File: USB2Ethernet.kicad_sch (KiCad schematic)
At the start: 35 parts, among them U17 LAN9512, U19 CAT250xxx, Y6 25Mhz

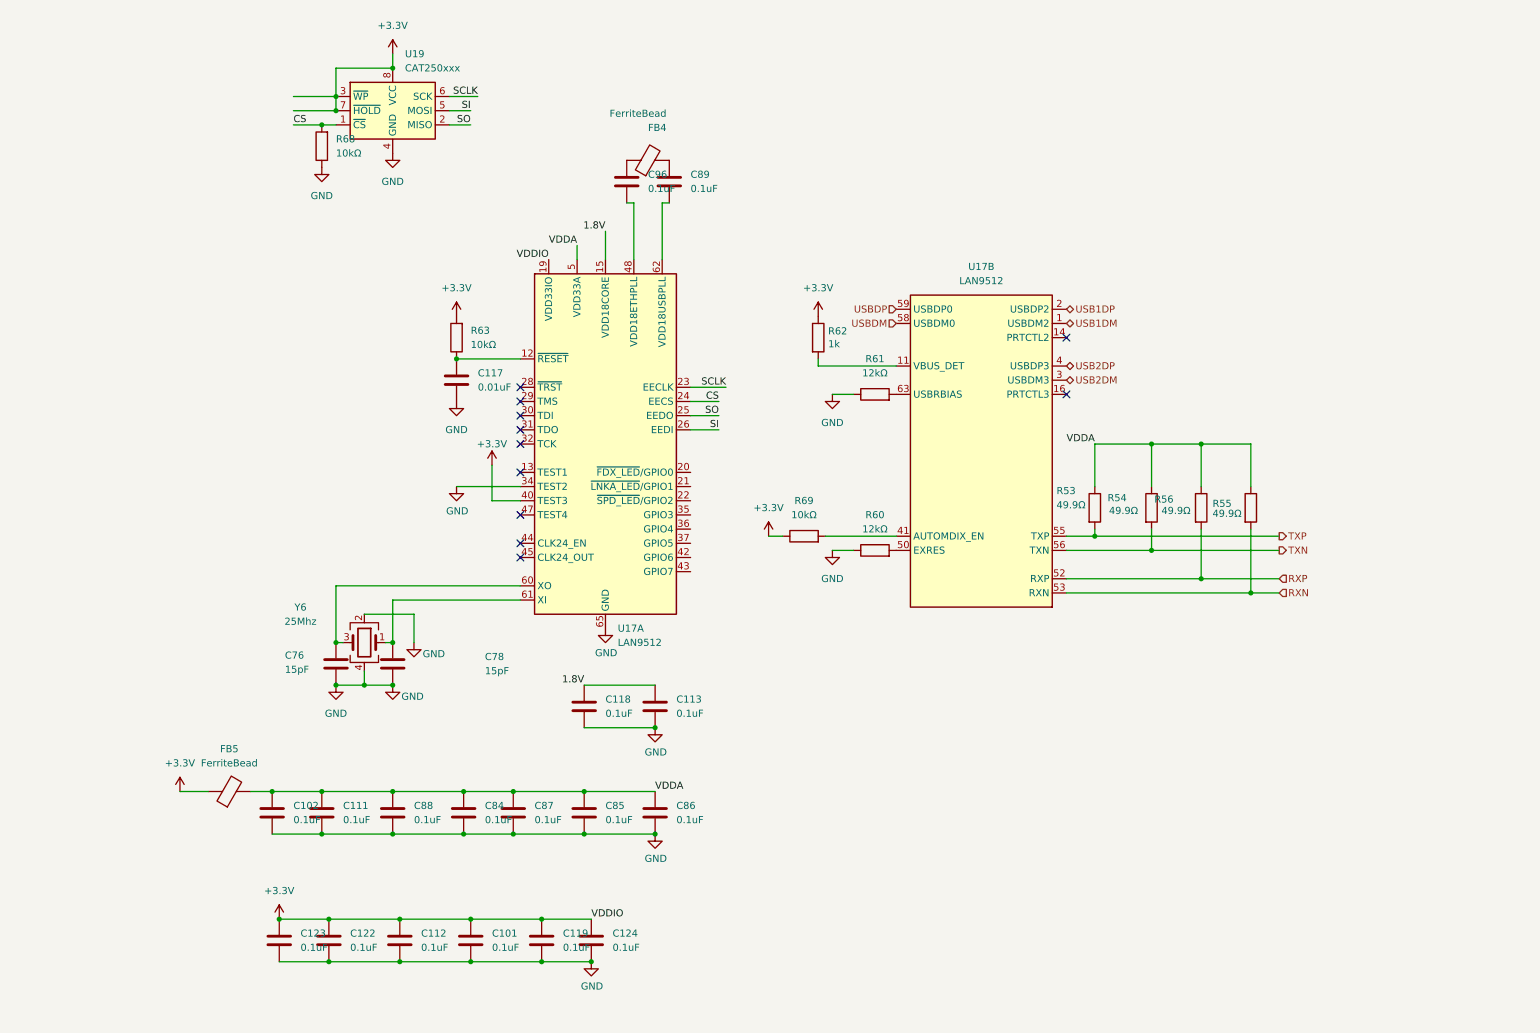
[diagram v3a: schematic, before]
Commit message: add sata capacitor
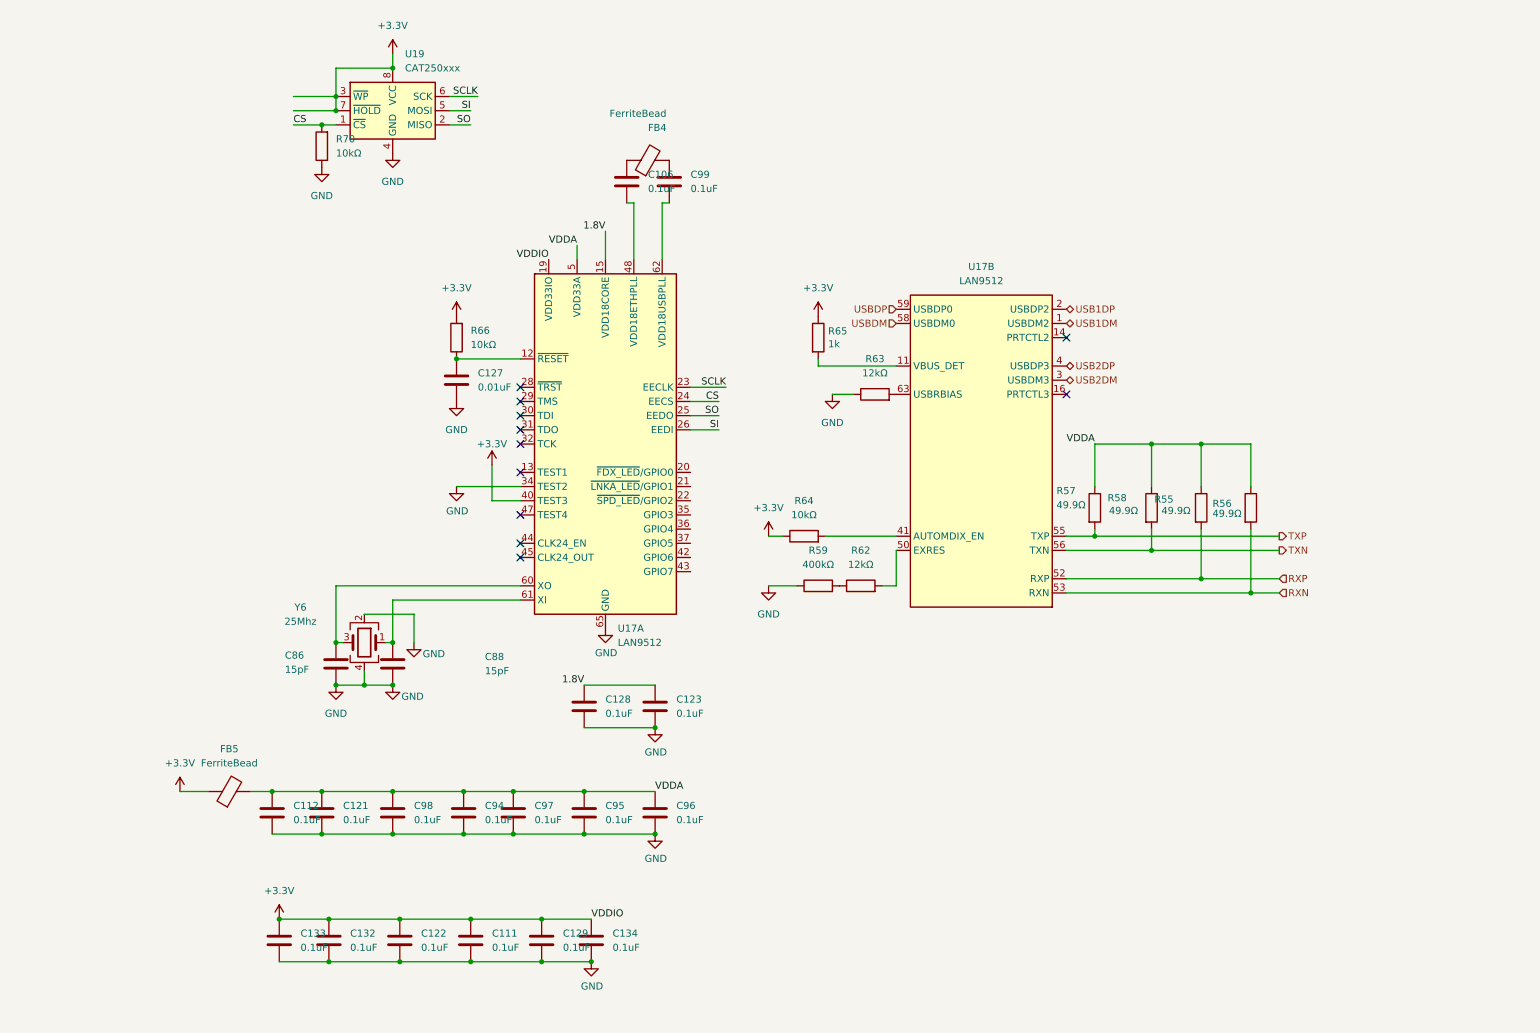
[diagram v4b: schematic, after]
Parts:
- added R59: 400kΩ, Resistor_SMD:R_0603_1608Metric_Pad0.98x0.95mm_HandSolder, symbol Device:R
- renumbered C96 to C106, C101 to C111, C102 to C112, C111 to C121, C112 to C122, C113 to C123, C117 to C127, C118 to C128, C119 to C129, C122 to C132, C123 to C133, C124 to C134, C76 to C86, C78 to C88, C84 to C94, C85 to C95, C86 to C96, C87 to C97, C88 to C98, C89 to C99, R56 to R55, R55 to R56, R53 to R57, R54 to R58, R60 to R62, R61 to R63, R69 to R64, R62 to R65, R63 to R66, R68 to R70
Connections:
- net GND: now also R59.1; no longer R62.1
- new net: R59.2, R62.1
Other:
- moved on the sheet: R62

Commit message: change design
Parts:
- renumbered C99 to C100, C94 to C95, C95 to C96, C96 to C97, C97 to C98, C98 to C99
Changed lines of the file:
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@@
 		(dnp no)
 		(fields_autoplaced yes)
-		(property "Reference" "C96"
+		(property "Reference" "C97"
 			(at 130.81 161.2899 0)
 			(effects
@@
 			(project "mainboard4"
 				(path "/dd07ab80-a59c-44f4-ac7d-849e21e1384e/3546f414-4018-45c7-a00a-bf02d214bf7f"
-					(reference "C96")
+					(reference "C97")
 					(unit 1)
 				)
@@
 		(dnp no)
 		(fields_autoplaced yes)
-		(property "Reference" "C95"
+		(property "Reference" "C96"
 			(at 118.11 161.2899 0)
 			(effects
@@
 			(project "mainboard4"
 				(path "/dd07ab80-a59c-44f4-ac7d-849e21e1384e/3546f414-4018-45c7-a00a-bf02d214bf7f"
-					(reference "C95")
+					(reference "C96")
 					(unit 1)
 				)
@@
 		(dnp no)
 		(fields_autoplaced yes)
-		(property "Reference" "C97"
+		(property "Reference" "C98"
 			(at 105.41 161.2899 0)
 			(effects
@@
 			(project "mainboard4"
 				(path "/dd07ab80-a59c-44f4-ac7d-849e21e1384e/3546f414-4018-45c7-a00a-bf02d214bf7f"
-					(reference "C97")
+					(reference "C98")
 					(unit 1)
 				)
@@
 		(dnp no)
 		(fields_autoplaced yes)
-		(property "Reference" "C98"
+		(property "Reference" "C99"
 			(at 83.82 161.2899 0)
 			(effects
@@
 			(project "mainboard4"
 				(path "/dd07ab80-a59c-44f4-ac7d-849e21e1384e/3546f414-4018-45c7-a00a-bf02d214bf7f"
-					(reference "C98")
+					(reference "C99")
 					(unit 1)
 				)
@@
 		(dnp no)
 		(fields_autoplaced yes)
-		(property "Reference" "C94"
+		(property "Reference" "C95"
 			(at 96.52 161.2899 0)
 			(effects
@@
 			(project "mainboard4"
 				(path "/dd07ab80-a59c-44f4-ac7d-849e21e1384e/3546f414-4018-45c7-a00a-bf02d214bf7f"
-					(reference "C94")
+					(reference "C95")
 					(unit 1)
 				)
@@
 		(dnp no)
 		(fields_autoplaced yes)
-		(property "Reference" "C99"
+		(property "Reference" "C100"
 			(at 133.35 48.2599 0)
 			(effects
@@
 			(project "mainboard4"
 				(path "/dd07ab80-a59c-44f4-ac7d-849e21e1384e/3546f414-4018-45c7-a00a-bf02d214bf7f"
-					(reference "C99")
+					(reference "C100")
 					(unit 1)
 				)

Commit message: add logp
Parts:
- renumbered C86 to C87, R55 to R52, R56 to R53, R57 to R54, R58 to R55, R59 to R57, R62 to R59, R63 to R61, R64 to R62, R65 to R63, R66 to R64, R70 to R68
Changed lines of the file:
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@@
 	(label "SI"
 		(at 138.43 93.98 180)
-		(fields_autoplaced yes)
 		(effects
 			(font
@@
 	(label "1.8V"
 		(at 118.11 58.42 180)
-		(fields_autoplaced yes)
 		(effects
 			(font
@@
 	(label "SO"
 		(at 93.98 39.37 180)
-		(fields_autoplaced yes)
 		(effects
 			(font
@@
 	(label "VDDA"
 		(at 113.03 60.96 180)
-		(fields_autoplaced yes)
 		(effects
 			(font
@@
 	(label "CS"
 		(at 62.23 39.37 0)
-		(fields_autoplaced yes)
 		(effects
 			(font
@@
 	(label "SCLK"
 		(at 95.25 34.29 180)
-		(fields_autoplaced yes)
 		(effects
 			(font
@@
 	(label "CS"
 		(at 138.43 88.9 180)
-		(fields_autoplaced yes)
 		(effects
 			(font
@@
 	(label "VDDA"
 		(at 127 158.75 0)
-		(fields_autoplaced yes)
 		(effects
 			(font
@@
 	(label "VDDIO"
 		(at 107.95 63.5 180)
-		(fields_autoplaced yes)
 		(effects
 			(font
@@
 	(label "SCLK"
 		(at 139.7 86.36 180)
-		(fields_autoplaced yes)
 		(effects
 			(font
@@
 	(label "1.8V"
 		(at 114.3 139.7 180)
-		(fields_autoplaced yes)
 		(effects
 			(font
@@
 	(label "SI"
 		(at 93.98 36.83 180)
-		(fields_autoplaced yes)
 		(effects
 			(font
@@
 	(label "SO"
 		(at 138.43 91.44 180)
-		(fields_autoplaced yes)
 		(effects
 			(font
@@
 	(label "VDDA"
 		(at 205.74 96.52 180)
-		(fields_autoplaced yes)
 		(effects
 			(font
@@
 	(label "VDDIO"
 		(at 115.57 181.61 0)
-		(fields_autoplaced yes)
 		(effects
 			(font
@@
 		(shape bidirectional)
 		(at 200.66 72.39 0)
-		(fields_autoplaced yes)
 		(effects
 			(font
@@
 		(shape bidirectional)
 		(at 200.66 82.55 0)
-		(fields_autoplaced yes)
 		(effects
 			(font
@@
 		(shape output)
 		(at 238.76 115.57 0)
-		(fields_autoplaced yes)
 		(effects
 			(font
@@
 		(shape input)
 		(at 238.76 123.19 0)
-		(fields_autoplaced yes)
 		(effects
 			(font
@@
 		(shape bidirectional)
 		(at 200.66 85.09 0)
-		(fields_autoplaced yes)
 		(effects
 			(font
@@
 		(shape bidirectional)
 		(at 200.66 74.93 0)
-		(fields_autoplaced yes)
 		(effects
 			(font
@@
 		(shape input)
 		(at 238.76 120.65 0)
-		(fields_autoplaced yes)
 		(effects
 			(font
@@
 		(shape output)
 		(at 238.76 113.03 0)
-		(fields_autoplaced yes)
 		(effects
 			(font
@@
 		(shape input)
 		(at 170.18 72.39 180)
-		(fields_autoplaced yes)
 		(effects
 			(font
@@
 		(shape input)
 		(at 170.18 74.93 180)
-		(fields_autoplaced yes)
 		(effects
 			(font
@@
 		(on_board yes)
 		(dnp no)
-		(property "Reference" "C86"
+		(property "Reference" "C87"
 			(at 60.706 134.366 0)
 			(effects
@@
 			(project "mainboard4"
 				(path "/dd07ab80-a59c-44f4-ac7d-849e21e1384e/3546f414-4018-45c7-a00a-bf02d214bf7f"
-					(reference "C86")
+					(reference "C87")
 					(unit 1)
 				)
@@
 		(on_board yes)
 		(dnp no)
-		(property "Reference" "R56"
+		(property "Reference" "R53"
 			(at 226.822 107.188 0)
 			(effects
@@
 			(project "mainboard4"
 				(path "/dd07ab80-a59c-44f4-ac7d-849e21e1384e/3546f414-4018-45c7-a00a-bf02d214bf7f"
-					(reference "R56")
+					(reference "R53")
 					(unit 1)
 				)
@@
 		(dnp no)
 		(fields_autoplaced yes)
-		(property "Reference" "R64"
+		(property "Reference" "R62"
 			(at 153.67 106.68 90)
 			(effects
@@
 			(project "mainboard4"
 				(path "/dd07ab80-a59c-44f4-ac7d-849e21e1384e/3546f414-4018-45c7-a00a-bf02d214bf7f"
-					(reference "R64")
+					(reference "R62")
 					(unit 1)
 				)
@@
 		(dnp no)
 		(fields_autoplaced yes)
-		(property "Reference" "R66"
+		(property "Reference" "R64"
 			(at 93.98 76.1999 0)
 			(effects
@@
 			(project "mainboard4"
 				(path "/dd07ab80-a59c-44f4-ac7d-849e21e1384e/3546f414-4018-45c7-a00a-bf02d214bf7f"
-					(reference "R66")
+					(reference "R64")
 					(unit 1)
 				)
@@
 		(on_board yes)
 		(dnp no)
-		(property "Reference" "R58"
+		(property "Reference" "R55"
 			(at 208.026 106.172 0)
 			(effects
@@
 			(project "mainboard4"
 				(path "/dd07ab80-a59c-44f4-ac7d-849e21e1384e/3546f414-4018-45c7-a00a-bf02d214bf7f"
-					(reference "R58")
+					(reference "R55")
 					(unit 1)
 				)
@@
 		(on_board yes)
 		(dnp no)
-		(property "Reference" "R57"
+		(property "Reference" "R54"
 			(at 198.882 104.902 0)
 			(effects
@@
 			(project "mainboard4"
 				(path "/dd07ab80-a59c-44f4-ac7d-849e21e1384e/3546f414-4018-45c7-a00a-bf02d214bf7f"
-					(reference "R57")
+					(reference "R54")
 					(unit 1)
 				)
@@
 		(dnp no)
 		(fields_autoplaced yes)
-		(property "Reference" "R70"
+		(property "Reference" "R68"
 			(at 69.85 41.9099 0)
 			(effects
@@
 			(project "mainboard4"
 				(path "/dd07ab80-a59c-44f4-ac7d-849e21e1384e/3546f414-4018-45c7-a00a-bf02d214bf7f"
-					(reference "R70")
+					(reference "R68")
 					(unit 1)
 				)
@@
 		(on_board yes)
 		(dnp no)
-		(property "Reference" "R55"
+		(property "Reference" "R52"
 			(at 216.408 106.426 0)
 			(effects
@@
 			(project "mainboard4"
 				(path "/dd07ab80-a59c-44f4-ac7d-849e21e1384e/3546f414-4018-45c7-a00a-bf02d214bf7f"
-					(reference "R55")
+					(reference "R52")
 					(unit 1)
 				)
@@
 		(dnp no)
 		(fields_autoplaced yes)
-		(property "Reference" "R59"
+		(property "Reference" "R57"
 			(at 156.21 115.57 90)
 			(effects
@@
 			(project "mainboard4"
 				(path "/dd07ab80-a59c-44f4-ac7d-849e21e1384e/3546f414-4018-45c7-a00a-bf02d214bf7f"
-					(reference "R59")
+					(reference "R57")
 					(unit 1)
 				)
@@
 		(dnp no)
 		(fields_autoplaced yes)
-		(property "Reference" "R62"
+		(property "Reference" "R59"
 			(at 163.83 115.57 90)
 			(effects
@@
 			(project "mainboard4"
 				(path "/dd07ab80-a59c-44f4-ac7d-849e21e1384e/3546f414-4018-45c7-a00a-bf02d214bf7f"
-					(reference "R62")
+					(reference "R59")
 					(unit 1)
 				)
@@
 		(dnp no)
 		(fields_autoplaced yes)
-		(property "Reference" "R63"
+		(property "Reference" "R61"
 			(at 166.37 81.28 90)
 			(effects
@@
 			(project "mainboard4"
 				(path "/dd07ab80-a59c-44f4-ac7d-849e21e1384e/3546f414-4018-45c7-a00a-bf02d214bf7f"
-					(reference "R63")
+					(reference "R61")
 					(unit 1)
 				)
@@
 		(on_board yes)
 		(dnp no)
-		(property "Reference" "R65"
+		(property "Reference" "R63"
 			(at 157.988 76.3016 0)
 			(effects
@@
 			(project "mainboard4"
 				(path "/dd07ab80-a59c-44f4-ac7d-849e21e1384e/3546f414-4018-45c7-a00a-bf02d214bf7f"
-					(reference "R65")
+					(reference "R63")
 					(unit 1)
 				)

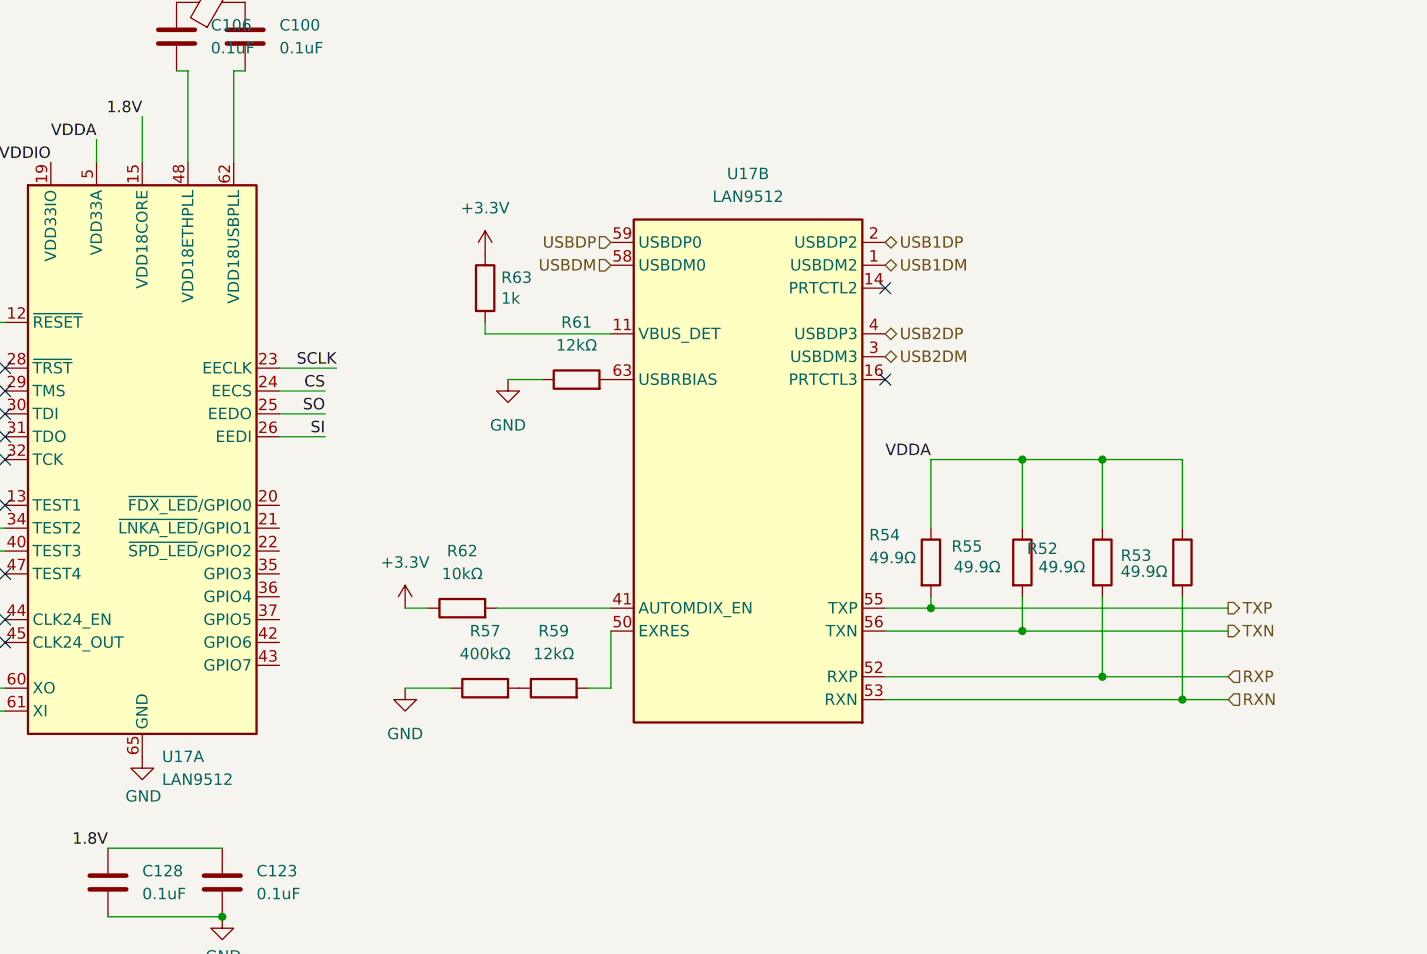
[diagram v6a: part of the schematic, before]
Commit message: delete USB connector
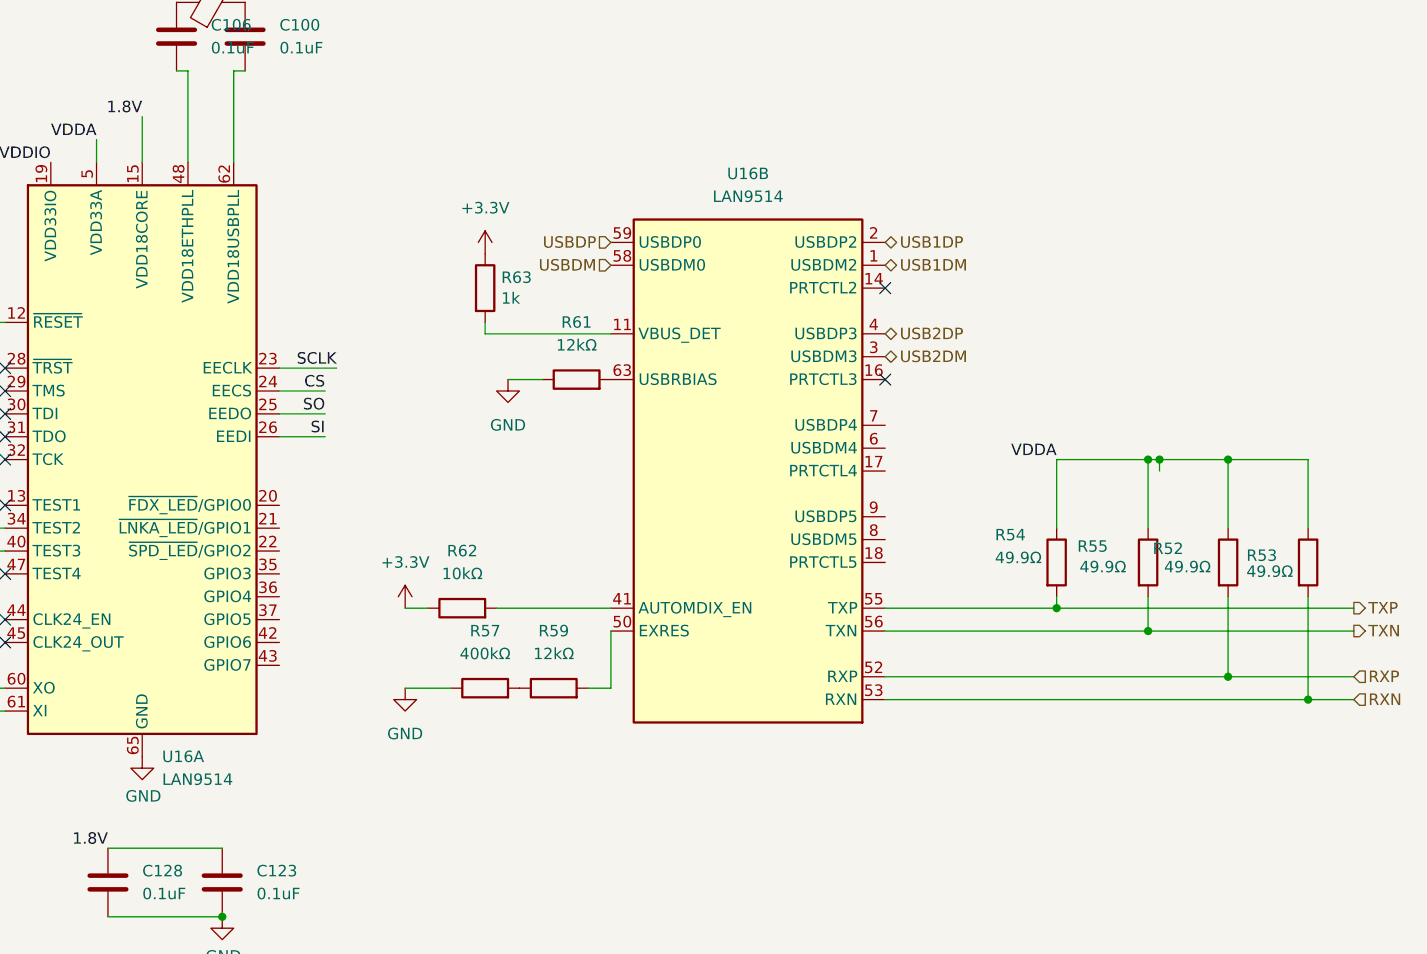
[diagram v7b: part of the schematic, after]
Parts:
- removed U17: LAN9512, Package_DFN_QFN:QFN-64-1EP_9x9mm_P0.5mm_EP7.3x7.3mm, symbol Interface_Ethernet:LAN9512
- added U16: LAN9514, Package_DFN_QFN:QFN-64-1EP_9x9mm_P0.5mm_EP7.3x7.3mm, symbol Interface_Ethernet:LAN9514
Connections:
- net +3.3V: now also U16.19 (VDD33IO), U16.27 (VDD33IO), U16.33 (VDD33IO), U16.39 (VDD33IO), U16.40 (TEST3), U16.46 (VDD33IO)
- net 1.8V: now also U16.15 (VDD18CORE), U16.38 (VDD18CORE)
- net CS: now also U16.24 (EECS)
- net GND: now also U16.34 (TEST2), U16.65 (GND)
- net RXN: now also U16.53 (RXN)
- net RXP: now also U16.52 (RXP)
- net SCLK: now also U16.23 (EECLK)
- net SI: now also U16.26 (EEDI)
- net SO: now also U16.25 (EEDO)
- net TXN: now also U16.56 (TXN)
- net TXP: now also U16.55 (TXP)
- net USB1DM: now also U16.1 (USBDM2)
- net USB1DP: now also U16.2 (USBDP2)
- net USB2DM: now also U16.3 (USBDM3)
- net USB2DP: now also U16.4 (USBDP3)
- net USBDM: now also U16.58 (USBDM0)
- net USBDP: now also U16.59 (USBDP0)
- net VDDA: now also U16.10 (VDD33A), U16.49 (VDD33A), U16.5 (VDD33A), U16.51 (VDD33A), U16.54 (VDD33A), U16.57 (VDD33A), U16.64 (VDD33A)
- net at C87.1, Y6.3: now also U16.60 (XO)
- net at C127.1, R64.1: now also U16.12 (~{RESET})
- net at C106.2: now also U16.48 (VDD18ETHPLL)
- net at C88.1, Y6.1: now also U16.61 (XI)
- net at C100.2: now also U16.62 (VDD18USBPLL)
- net at R62.2: now also U16.41 (AUTOMDIX_EN)
- net at R63.2: now also U16.11 (VBUS_DET)
- net at R59.2: now also U16.50 (EXRES)
- net at R61.2: now also U16.63 (USBRBIAS)
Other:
- moved on the sheet: R52, R53, R54, R55
